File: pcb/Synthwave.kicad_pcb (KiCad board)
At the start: 2 copper layers, 72.4 x 112.8 mm, 62 parts, among them J1 Barrel_Jack_Switch, J11 Conn_01x04_Socket, J12 Conn_01x04_Socket, J2 Conn_01x06_Socket, J3 SDA, J4 Conn_01x06_Socket, J5 ADC3, J6 ADC4, J7 Conn_01x04_Socket, J8 Conn_01x04_Socket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

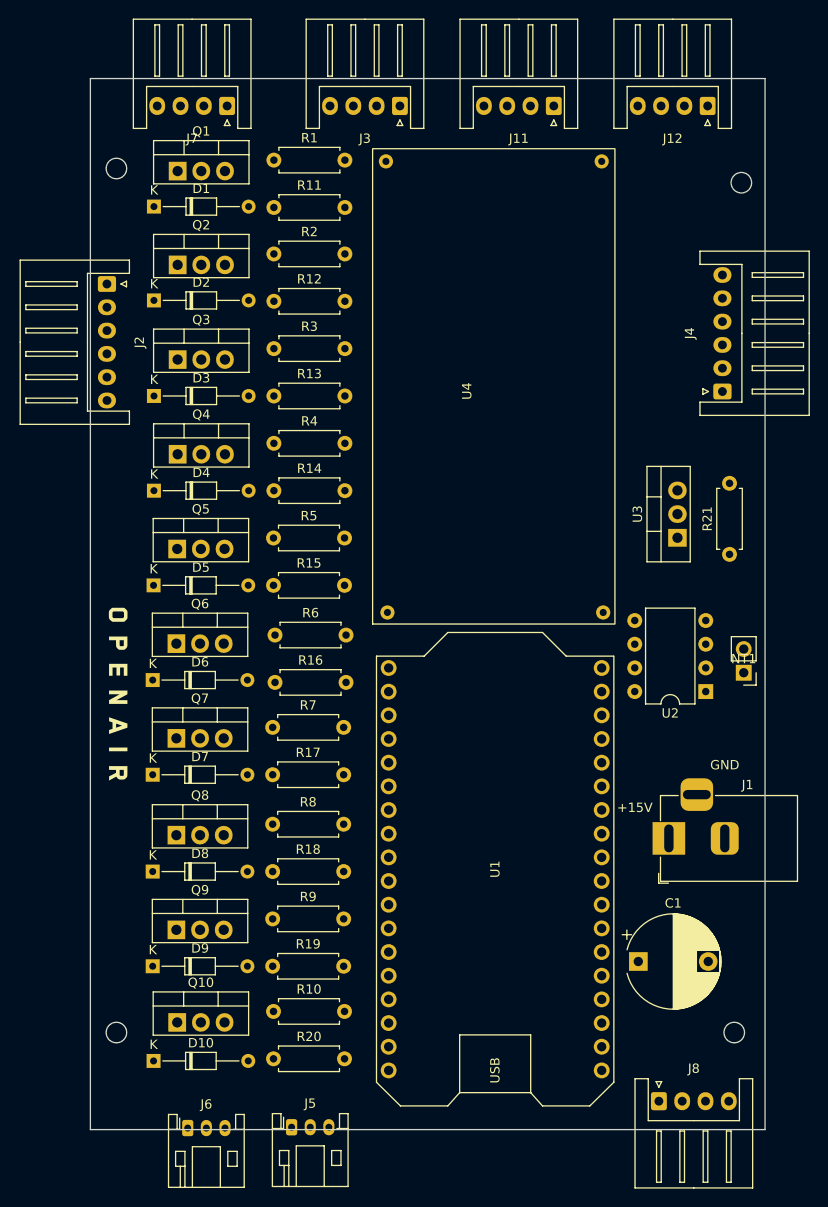
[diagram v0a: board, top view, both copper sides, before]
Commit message: Finish autorouting.  Updates to electrode holder and container cover
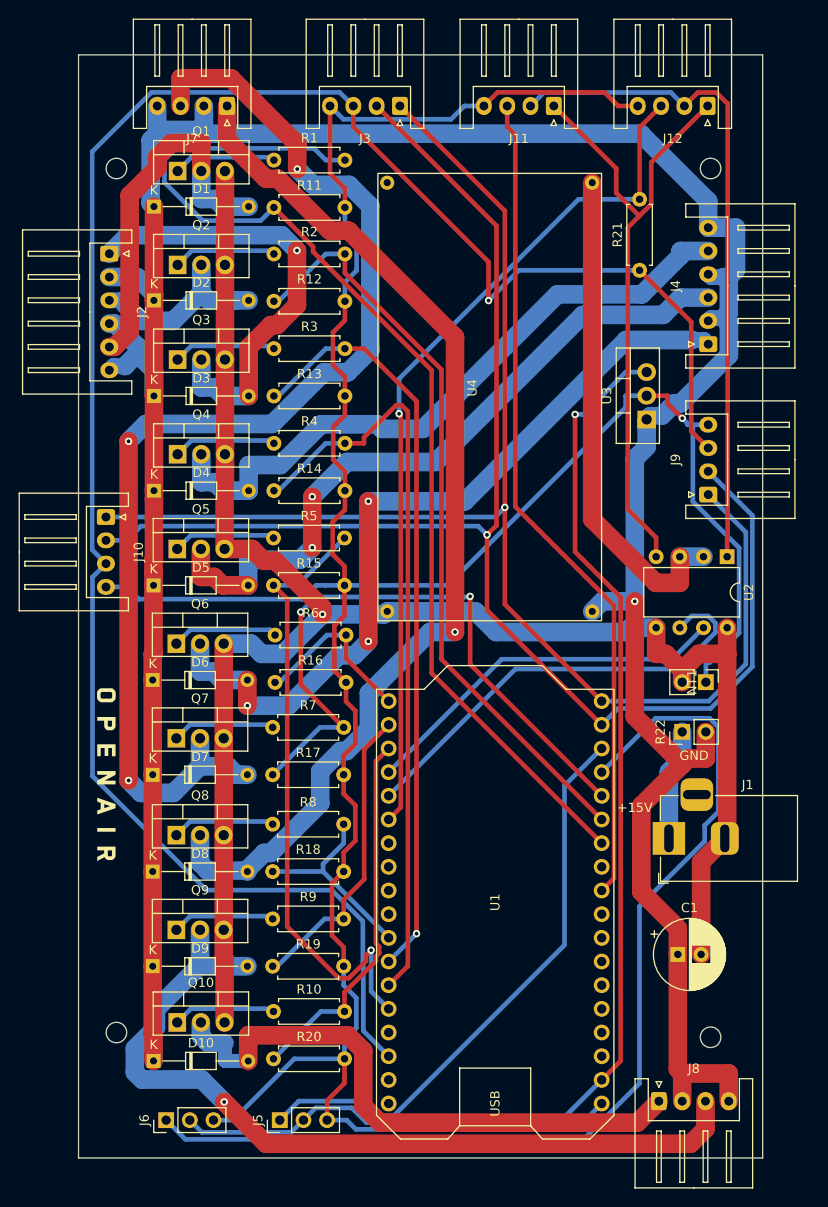
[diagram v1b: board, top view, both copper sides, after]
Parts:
- added J10: SDA, Connector_JST:JST_XH_S4B-XH-A_1x04_P2.50mm_Horizontal, F.Cu at (18.2, 59.0)
- added J9: SDA, Connector_JST:JST_XH_S4B-XH-A_1x04_P2.50mm_Horizontal, F.Cu at (82.8, 56.6)
- added R22: 0R, Connector_PinHeader_2.54mm:PinHeader_1x02_P2.54mm_Vertical, F.Cu at (80.0, 82.0)
- C1: footprint Capacitor_THT:CP_Radial_D10.0mm_P7.50mm -> Capacitor_THT:CP_Radial_D7.5mm_P2.50mm
- J11: value Conn_01x04_Socket -> ELEC1 FLOAT1
- J5, J6: footprint Connector_JST:JST_PH_S3B-PH-K_1x03_P2.00mm_Horizontal -> Connector_PinHeader_2.54mm:PinHeader_1x03_P2.54mm_Vertical
- moved R21 32.0 mm to (75.4, 32.5)
- moved U2 14.6 mm to (84.8, 63.2), turned to -90 degrees
- moved U3 13.1 mm to (76.2, 48.5)
- moved G*** 8.73 mm to (18.3, 86.4)
- moved J4 5.30 mm to (82.8, 40.4)
- moved C1 4.31 mm to (79.5, 105.9)
- moved NT1 4.19 mm to (82.5, 76.7), turned to -90 degrees
- moved H4 3.64 mm to (83.1, 21.6)
- moved U1 3.56 mm to (59.9, 100.3)
- moved J2 3.26 mm to (18.5, 30.7)
- moved H3 2.59 mm to (83.1, 114.8)
- moved J6 2.47 mm to (24.6, 123.7), turned to 90 degrees
- moved J5 1.48 mm to (36.8, 123.7), turned to 90 degrees
- moved U4 0.67 mm to (47.4, 70.1)
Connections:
- C1 pad 1: +15V -> /Device Power
- D1 pad 1: +15V -> /Device Power
- D10 pad 1: +15V -> /Device Power
- D2 pad 1: +15V -> /Device Power
- D3 pad 1: +15V -> /Device Power
- D4 pad 1: +15V -> /Device Power
- D5 pad 1: +15V -> /Device Power
- D6 pad 1: +15V -> /Device Power
- D7 pad 1: +15V -> /Device Power
- D8 pad 1: +15V -> /Device Power
- D9 pad 1: +15V -> /Device Power
- J2 pad 2: +15V -> /Device Power
- J2 pad 4: +15V -> /Device Power
- J2 pad 6: +15V -> /Device Power
- J4 pad 2: +15V -> /Device Power
- J4 pad 4: +15V -> /Device Power
- J4 pad 6: +15V -> /Device Power
- J7 pad 2: +15V -> /Device Power
- J7 pad 4: +15V -> /Device Power
- J8 pad 2: +15V -> /Device Power
- J8 pad 4: +15V -> /Device Power
- U3 pad 1: +15V -> /Device Power
- U4 pad 4: +15V -> /Device Power
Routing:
- net /Device Power: track 0.00 -> 322.4 mm, vias 0 -> 1
- net GND1: track 0.00 -> 310.9 mm, vias 0 -> 1
- net Net-(J10-Pin_3): track 0.00 -> 217.1 mm, vias 0 -> 1
- net GND: track 0.00 -> 194.3 mm, vias 0 -> 1
- net Net-(J10-Pin_2): track 0.00 -> 160.8 mm, vias 0 -> 1
- net Net-(J10-Pin_1): track 0.00 -> 153.0 mm, vias 0 -> 1
- net +5V: track 0.00 -> 132.2 mm, vias 0 -> 1
- net Net-(D7-A): track 0.00 -> 130.3 mm, vias 0 -> 3
- net Net-(U1-7_ADC): track 0.00 -> 119.6 mm
- net Net-(D8-A): track 0.00 -> 114.2 mm, vias 0 -> 1
- net Net-(J6-Pin_1): track 0.00 -> 111.2 mm
- net Net-(J12-Pin_3): track 0.00 -> 92.7 mm, vias 0 -> 1
- net Net-(D9-A): track 0.00 -> 91.4 mm, vias 0 -> 1
- net Net-(J11-Pin_3): track 0.00 -> 89.5 mm
- net Net-(D6-A): track 0.00 -> 85.9 mm, vias 0 -> 3
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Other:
- board size 72.4 x 112.8 mm -> 73.4 x 118.4 mm
